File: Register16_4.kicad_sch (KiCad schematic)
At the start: 4 parts

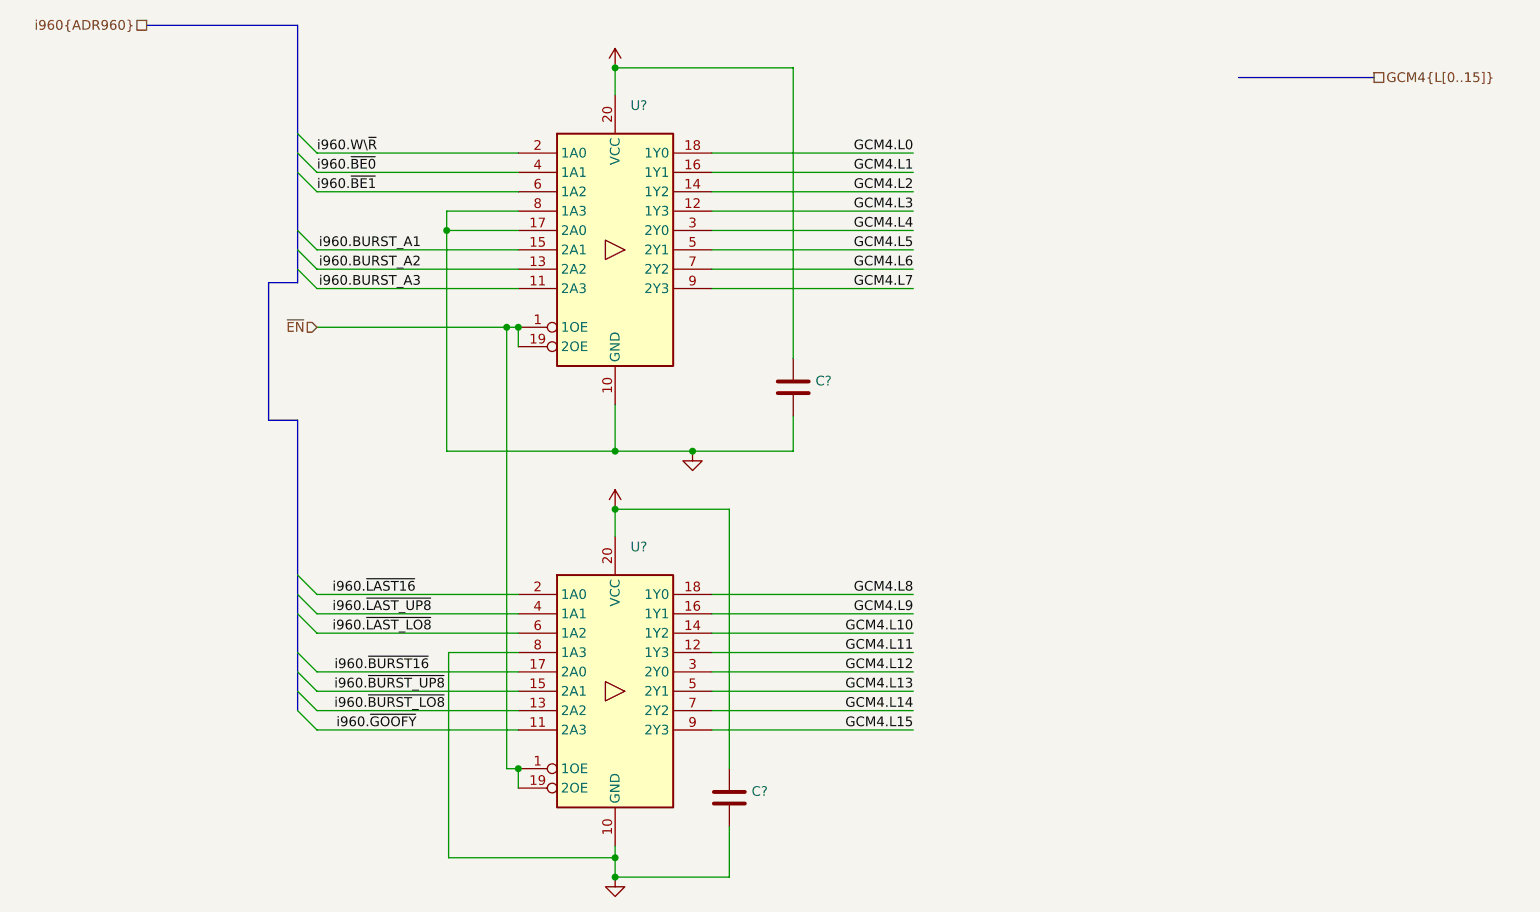
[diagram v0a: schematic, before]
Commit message: Added the LOW global label
Simplify things
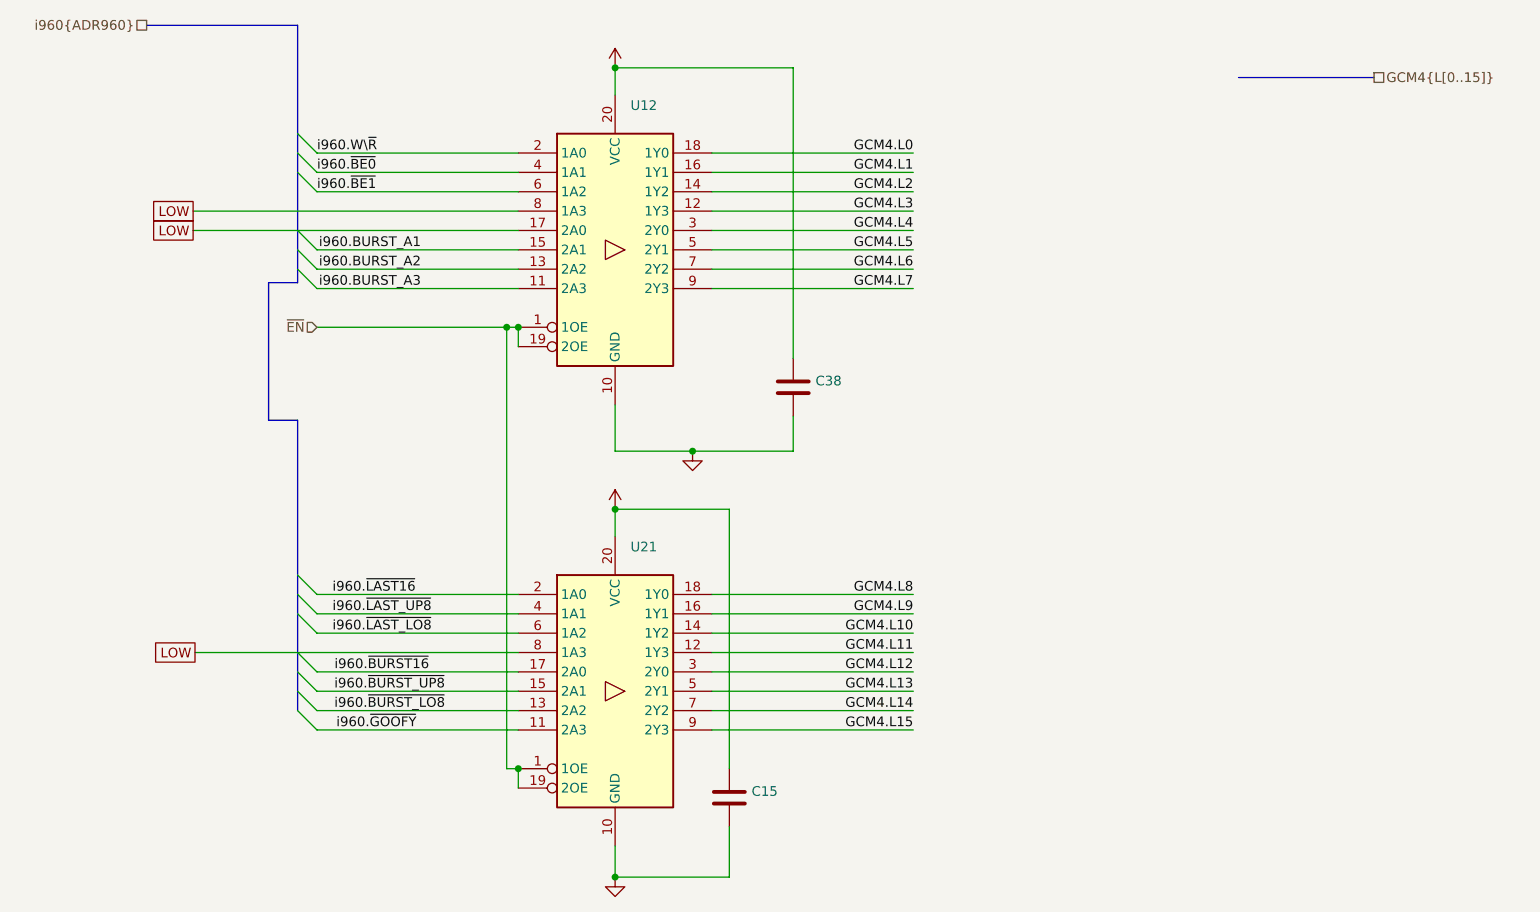
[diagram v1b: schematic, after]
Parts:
- gave numbers to parts that had none: 4
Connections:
- net GND: no longer U12.17 (2A0), U12.8 (1A3), U21.8 (1A3)
- new net LOW: U12.17 (2A0), U12.8 (1A3), U21.8 (1A3)
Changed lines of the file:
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@@
   (junction (at 128.016 62.992) (diameter 0) (color 0 0 0 0)
   )
-  (junction (at 142.24 132.588) (diameter 0) (color 0 0 0 0)
-  )
   (junction (at 142.24 86.868) (diameter 0) (color 0 0 0 0)
   )
-  (junction (at 142.24 79.248) (diameter 0) (color 0 0 0 0)
-  )
   (junction (at 129.54 120.904) (diameter 0) (color 0 0 0 0)
   )
   (junction (at 152.4 79.248) (diameter 0) (color 0 0 0 0)
   )
-  (junction (at 120.142 50.292) (diameter 0) (color 0 0 0 0)
-  )
   (junction (at 142.24 135.128) (diameter 0) (color 0 0 0 0)
   )
@@
     (stroke (width 0) (type default) (color 0 0 0 0))
   )
-  (wire (pts (xy 129.54 105.664) (xy 120.396 105.664))
+  (wire (pts (xy 100.584 105.664) (xy 129.54 105.664))
     (stroke (width 0) (type default) (color 0 0 0 0))
   )
@@
     (stroke (width 0) (type default) (color 0 0 0 0))
   )
-  (wire (pts (xy 120.396 132.588) (xy 142.24 132.588))
-    (stroke (width 0) (type default) (color 0 0 0 0))
-  )
   (wire (pts (xy 142.24 28.956) (xy 142.24 32.512))
     (stroke (width 0) (type default) (color 0 0 0 0))
@@
     (stroke (width 0) (type default) (color 0 0 0 0))
   )
-  (wire (pts (xy 120.142 79.248) (xy 142.24 79.248))
+  (wire (pts (xy 86.868 50.292) (xy 100.584 50.292))
     (stroke (width 0) (type default) (color 0 0 0 0))
   )
@@
     (stroke (width 0) (type default) (color 0 0 0 0))
   )
-  (wire (pts (xy 142.24 132.588) (xy 142.24 131.064))
+  (wire (pts (xy 142.24 131.064) (xy 142.24 135.128))
     (stroke (width 0) (type default) (color 0 0 0 0))
   )
@@
     (stroke (width 0) (type default) (color 0 0 0 0))
   )
-  (wire (pts (xy 120.142 50.292) (xy 129.54 50.292))
-    (stroke (width 0) (type default) (color 0 0 0 0))
-  )
-  (wire (pts (xy 120.142 50.292) (xy 120.142 79.248))
-    (stroke (width 0) (type default) (color 0 0 0 0))
-  )
   (bus (pts (xy 100.584 108.204) (xy 100.584 105.664))
     (stroke (width 0) (type default) (color 0 0 0 0))
@@
     (stroke (width 0) (type default) (color 0 0 0 0))
   )
+  (wire (pts (xy 86.868 47.752) (xy 129.54 47.752))
+    (stroke (width 0) (type default) (color 0 0 0 0))
+  )
   (wire (pts (xy 142.24 79.248) (xy 152.4 79.248))
     (stroke (width 0) (type default) (color 0 0 0 0))
@@
     (stroke (width 0) (type default) (color 0 0 0 0))
   )
-  (wire (pts (xy 120.142 47.752) (xy 120.142 50.292))
-    (stroke (width 0) (type default) (color 0 0 0 0))
-  )
-  (wire (pts (xy 129.54 47.752) (xy 120.142 47.752))
+  (wire (pts (xy 87.122 105.664) (xy 100.584 105.664))
     (stroke (width 0) (type default) (color 0 0 0 0))
   )
@@
     (stroke (width 0) (type default) (color 0 0 0 0))
   )
-  (wire (pts (xy 142.24 135.128) (xy 142.24 132.588))
-    (stroke (width 0) (type default) (color 0 0 0 0))
-  )
   (bus (pts (xy 100.584 40.132) (xy 100.584 37.592))
     (stroke (width 0) (type default) (color 0 0 0 0))
   )
-  (wire (pts (xy 120.396 105.664) (xy 120.396 132.588))
-    (stroke (width 0) (type default) (color 0 0 0 0))
-  )
   (bus (pts (xy 100.584 57.15) (xy 100.584 55.372))
     (stroke (width 0) (type default) (color 0 0 0 0))
   )
+  (wire (pts (xy 100.584 50.292) (xy 129.54 50.292))
+    (stroke (width 0) (type default) (color 0 0 0 0))
+  )
   (label "GCM4.L8" (at 181.356 98.044 180)
     (effects (font (size 1.27 1.27)) (justify right bottom))
@@
   (label "i960.~{BE1}" (at 103.124 45.212 0)
     (effects (font (size 1.27 1.27)) (justify left bottom))
+  )
+  (global_label "LOW" (shape passive) (at 87.122 105.664 180) (fields_autoplaced)
+    (effects (font (size 1.27 1.27)) (justify right))
+    (property "Intersheet References" "${INTERSHEET_REFS}" (id 0) (at 80.9878 105.5846 0)
+      (effects (font (size 1.27 1.27)) (justify right) hide)
+    )
+  )
+  (global_label "LOW" (shape passive) (at 86.868 47.752 180) (fields_autoplaced)
+    (effects (font (size 1.27 1.27)) (justify right))
+    (property "Intersheet References" "${INTERSHEET_REFS}" (id 0) (at 80.7338 47.6726 0)
+      (effects (font (size 1.27 1.27)) (justify right) hide)
+    )
+  )
+  (global_label "LOW" (shape passive) (at 86.868 50.292 180) (fields_autoplaced)
+    (effects (font (size 1.27 1.27)) (justify right))
+    (property "Intersheet References" "${INTERSHEET_REFS}" (id 0) (at 80.7338 50.2126 0)
+      (effects (font (size 1.27 1.27)) (justify right) hide)
+    )
   )
   (hierarchical_label "i960{ADR960}" (shape passive) (at 80.772 23.368 180)
@@
   (symbol (lib_id "power:VCC") (at 142.24 86.868 0) (unit 1)
     (in_bom yes) (on_board yes) (fields_autoplaced)
-    (property "Reference" "#PWR?" (id 0) (at 142.24 90.678 0)
+    (property "Reference" "#PWR02" (id 0) (at 142.24 90.678 0)
       (effects (font (size 1.27 1.27)) hide)
     )
@@
   (symbol (lib_id "power:GND") (at 142.24 135.128 0) (unit 1)
     (in_bom yes) (on_board yes) (fields_autoplaced)
-    (property "Reference" "#PWR?" (id 0) (at 142.24 141.478 0)
+    (property "Reference" "#PWR03" (id 0) (at 142.24 141.478 0)
       (effects (font (size 1.27 1.27)) hide)
     )
@@
   (symbol (lib_id "power:GND") (at 152.4 79.248 0) (unit 1)
     (in_bom yes) (on_board yes) (fields_autoplaced)
-    (property "Reference" "#PWR?" (id 0) (at 152.4 85.598 0)
+    (property "Reference" "#PWR04" (id 0) (at 152.4 85.598 0)
       (effects (font (size 1.27 1.27)) hide)
     )
@@
   (symbol (lib_id "Device:C") (at 157.226 124.714 0) (unit 1)
     (in_bom yes) (on_board yes) (fields_autoplaced)
-    (property "Reference" "C?" (id 0) (at 160.147 123.8793 0)
+    (property "Reference" "C15" (id 0) (at 160.147 123.8793 0)
       (effects (font (size 1.27 1.27)) (justify left))
     )
@@
   (symbol (lib_id "Device:C") (at 165.608 70.866 0) (unit 1)
     (in_bom yes) (on_board yes) (fields_autoplaced)
-    (property "Reference" "C?" (id 0) (at 168.529 70.0313 0)
+    (property "Reference" "C38" (id 0) (at 168.529 70.0313 0)
       (effects (font (size 1.27 1.27)) (justify left))
     )
@@
   (symbol (lib_id "74xx:74HC244") (at 142.24 110.744 0) (unit 1)
     (in_bom yes) (on_board yes) (fields_autoplaced)
-    (property "Reference" "U?" (id 0) (at 144.2594 91.8042 0)
+    (property "Reference" "U21" (id 0) (at 144.2594 91.8042 0)
       (effects (font (size 1.27 1.27)) (justify left))
     )
@@
   (symbol (lib_id "power:VCC") (at 142.24 28.956 0) (unit 1)
     (in_bom yes) (on_board yes) (fields_autoplaced)
-    (property "Reference" "#PWR?" (id 0) (at 142.24 32.766 0)
+    (property "Reference" "#PWR01" (id 0) (at 142.24 32.766 0)
       (effects (font (size 1.27 1.27)) hide)
     )
@@
   (symbol (lib_id "74xx:74HC244") (at 142.24 52.832 0) (unit 1)
     (in_bom yes) (on_board yes) (fields_autoplaced)
-    (property "Reference" "U?" (id 0) (at 144.2594 33.8922 0)
-      (effects (font (size 1.27 1.27)) (justify left))
-    )
+    (property "Reference" "U12" (id 0) (at 144.2594 33.8922 0)
+      (effects (font (size 1.27 1.27)) (justify left))
+    )

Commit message: use the output enable lines on the latches and buffers to do direct logic level conversion
Save some chips in the process.
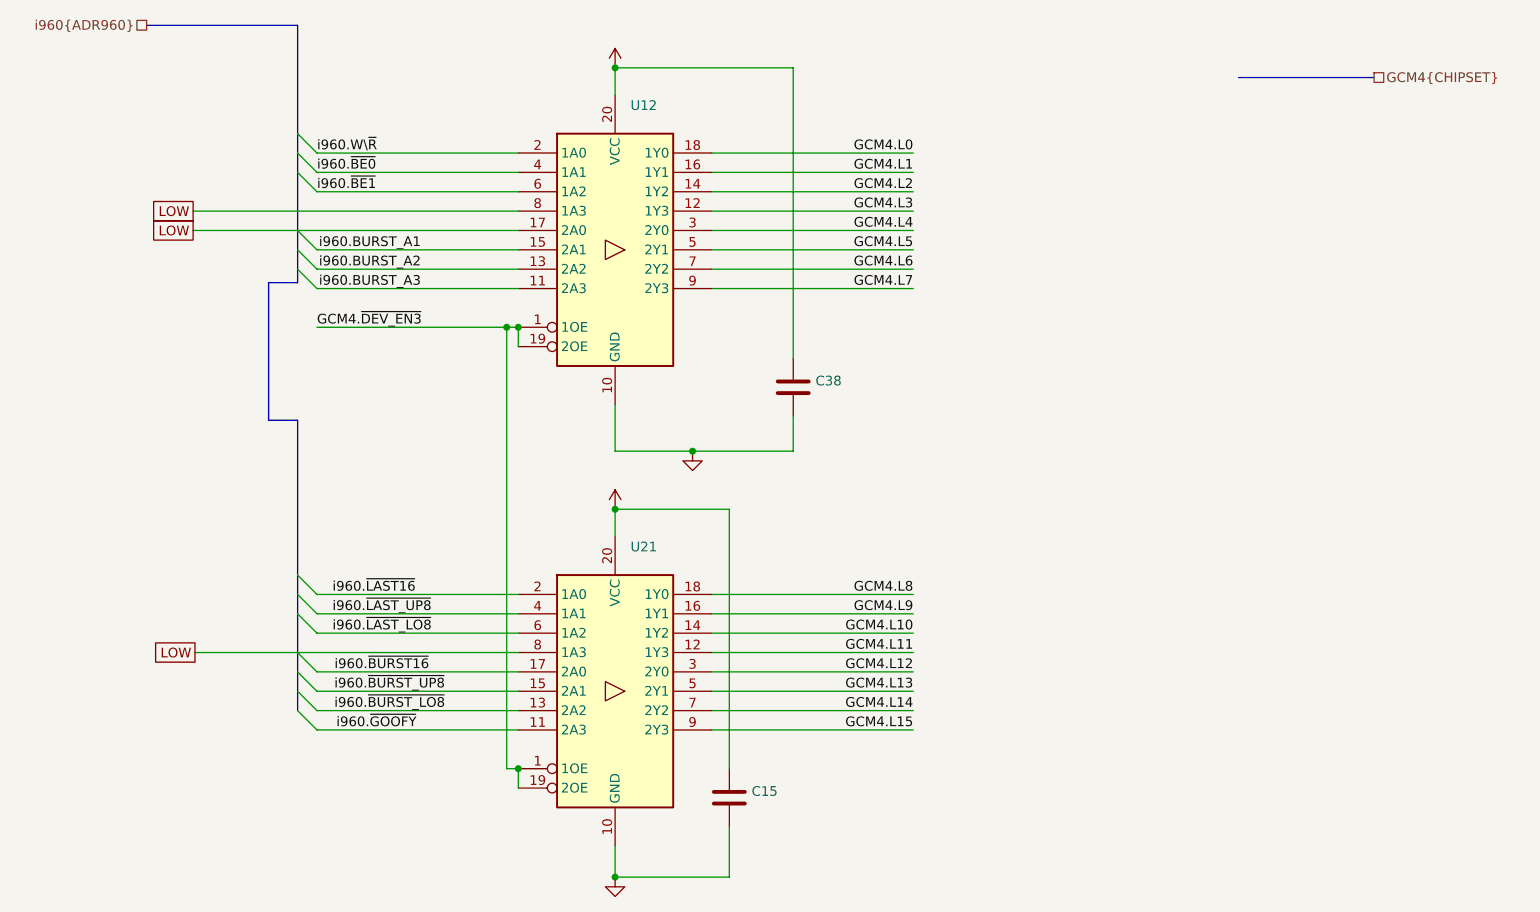
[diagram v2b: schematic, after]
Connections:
- net ~{EN} renamed GCM4.~{DEV_EN3}
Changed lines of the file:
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@@
     (effects (font (size 1.27 1.27)) (justify right bottom))
+  )
+  (label "GCM4.~{DEV_EN3}" (at 103.124 62.992 0)
+    (effects (font (size 1.27 1.27)) (justify left bottom))
   )
   (label "i960.BURST_A1" (at 103.378 52.832 0)
@@
     (effects (font (size 1.27 1.27)) (justify right))
   )
-  (hierarchical_label "GCM4{L[0..15]}" (shape passive) (at 241.808 30.226 0)
+  (hierarchical_label "GCM4{CHIPSET}" (shape passive) (at 241.808 30.226 0)
     (effects (font (size 1.27 1.27)) (justify left))
   )
-  (hierarchical_label "~{EN}" (shape input) (at 103.124 62.992 180)
-    (effects (font (size 1.27 1.27)) (justify right))
-  )
   (symbol (lib_id "power:VCC") (at 142.24 86.868 0) (unit 1)

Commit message: Use individual resistors for better layout purposes
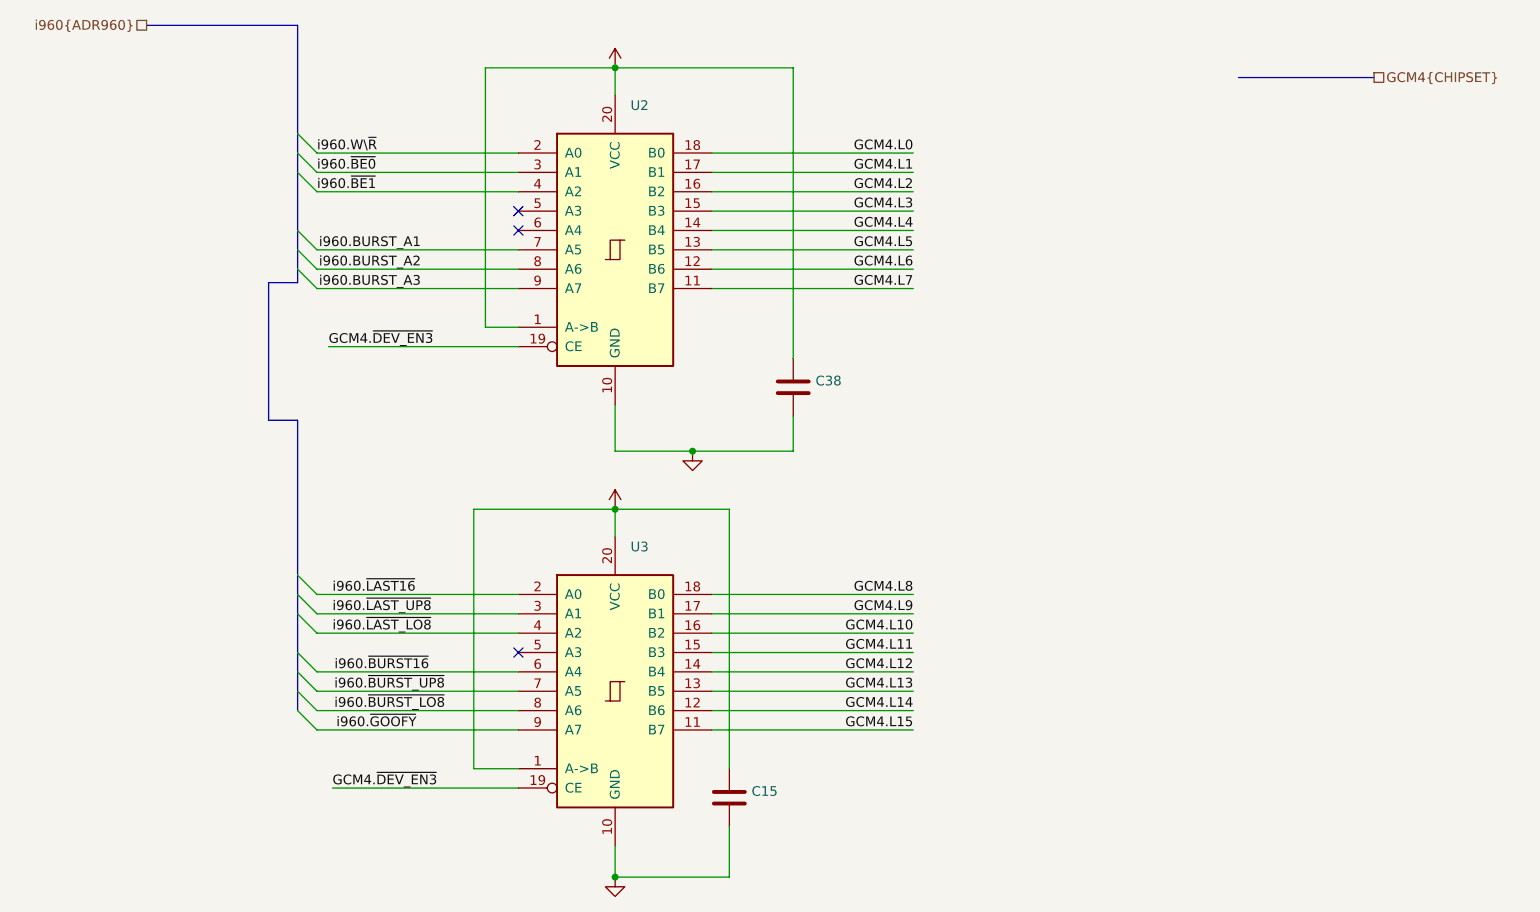
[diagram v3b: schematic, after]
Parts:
- removed U12, U21: (no value), symbol 74xx:74HC244
- added U2, U3: (no value), symbol 74xx:74HC245
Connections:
- net GCM4.L0: now also U2.18 (B0)
- net GCM4.L1: now also U2.17 (B1)
- net GCM4.L10: now also U3.16 (B2)
- net GCM4.L11: now also U3.15 (B3)
- net GCM4.L12: now also U3.14 (B4)
- net GCM4.L13: now also U3.13 (B5)
- net GCM4.L14: now also U3.12 (B6)
- net GCM4.L15: now also U3.11 (B7)
- net GCM4.L2: now also U2.16 (B2)
- net GCM4.L3: now also U2.15 (B3)
- net GCM4.L4: now also U2.14 (B4)
- net GCM4.L5: now also U2.13 (B5)
- net GCM4.L6: now also U2.12 (B6)
- net GCM4.L7: now also U2.11 (B7)
- net GCM4.L8: now also U3.18 (B0)
- net GCM4.L9: now also U3.17 (B1)
- net GCM4.~{DEV_EN3}: now also U2.19 (CE), U3.19 (CE)
- net GND: now also U2.10 (GND), U3.10 (GND)
- net VCC: now also U2.1 (A->B), U2.20 (VCC), U3.1 (A->B), U3.20 (VCC)
- net i960.BURST_A1: now also U2.7 (A5)
- net i960.BURST_A2: now also U2.8 (A6)
- net i960.BURST_A3: now also U2.9 (A7)
- net i960.W\~{R}: now also U2.2 (A0)
- net i960.~{BE0}: now also U2.3 (A1)
- net i960.~{BE1}: now also U2.4 (A2)
- net i960.~{BURST16}: now also U3.6 (A4)
- net i960.~{BURST_LO8}: now also U3.8 (A6)
- net i960.~{BURST_UP8}: now also U3.7 (A5)
- net i960.~{GOOFY}: now also U3.9 (A7)
- net i960.~{LAST16}: now also U3.2 (A0)
- net i960.~{LAST_LO8}: now also U3.4 (A2)
- net i960.~{LAST_UP8}: now also U3.3 (A1)
- no-connect marks 0 -> 3
